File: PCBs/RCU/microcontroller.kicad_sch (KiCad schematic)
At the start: 24 parts, among them J200 USB_C_Receptacle_USB2.0, J201 Conn_01x05, SW201 SW_Push, U200 STM32G0B1CBT6, U201 USBLC6-2SC6, Y200 16MHz

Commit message: Schematic cleanup
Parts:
- C202: value 0.1u -> (none)
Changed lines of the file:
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@@
       (effects (font (size 1.27 1.27)) (justify left))
     )
-    (property "Value" "0.1u" (id 1) (at 180.34 132.0799 0)
+    (property "Value" "" (id 1) (at 180.34 132.0799 0)
       (effects (font (size 1.27 1.27)) (justify left))
     )

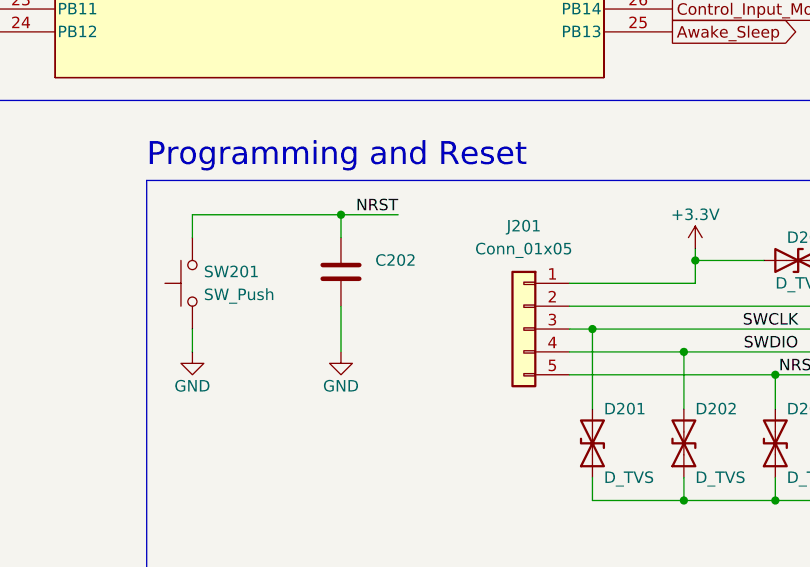
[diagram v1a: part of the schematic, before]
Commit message: Corrected SPI_MOSI and SPI_MISO labels on U700 - external memory
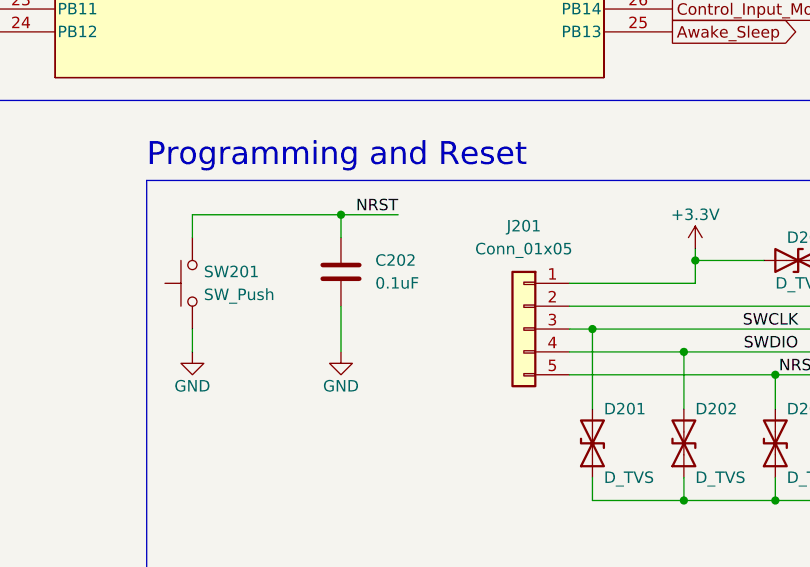
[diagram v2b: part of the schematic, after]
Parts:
- C202: value (none) -> 0.1uF
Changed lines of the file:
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@@
       (effects (font (size 1.27 1.27)) (justify left))
     )
-    (property "Value" "" (id 1) (at 180.34 132.0799 0)
+    (property "Value" "0.1uF" (id 1) (at 180.34 132.0799 0)
       (effects (font (size 1.27 1.27)) (justify left))
     )

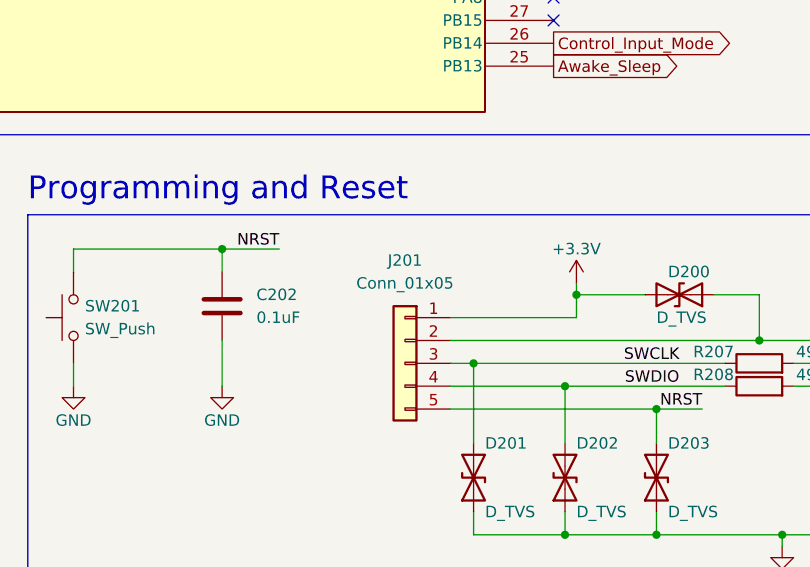
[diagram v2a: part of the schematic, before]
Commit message: Add microcontroller, USB receptable and Connx05 footprints
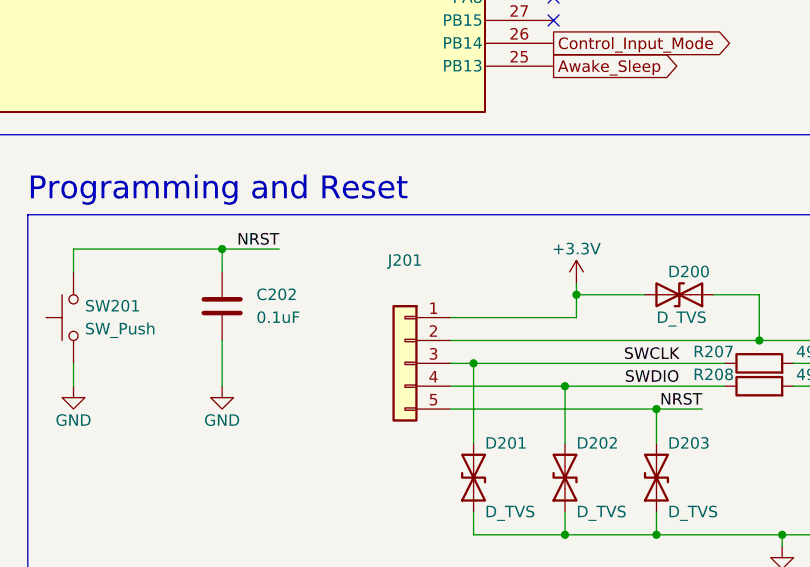
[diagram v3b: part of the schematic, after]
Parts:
- J200: footprint (none) -> Connector_USB:USB_C_Receptacle_HRO_TYPE-C-31-M-12
- J201: value Conn_01x05 -> (none)
- U200: footprint LQFP48_STM32G0B1CBT_STM -> Package_QFP:LQFP-48-1EP_7x7mm_P0.5mm_EP3.6x3.6mm
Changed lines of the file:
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@@
     (in_bom yes) (on_board yes) (fields_autoplaced)
     (property "Reference" "J201" (id 0) (at 196.85 125.73 0))
-    (property "Value" "Conn_01x05" (id 1) (at 196.85 128.27 0))
+    (property "Value" "" (id 1) (at 196.85 128.27 0))
     (property "Footprint" "" (id 2) (at 196.85 137.16 0)
       (effects (font (size 1.27 1.27)) hide)
@@
       (effects (font (size 1.524 1.524)))
     )
-    (property "Footprint" "LQFP48_STM32G0B1CBT_STM" (id 2) (at 137.16 45.72 0)
+    (property "Footprint" "Package_QFP:LQFP-48-1EP_7x7mm_P0.5mm_EP3.6x3.6mm" (id 2) (at 137.16 45.72 0)
       (effects (font (size 1.27 1.27) italic) hide)
     )
@@
     (property "Reference" "J200" (id 0) (at 60.96 133.35 0))
     (property "Value" "USB_C_Receptacle_USB2.0" (id 1) (at 60.96 135.89 0))
-    (property "Footprint" "" (id 2) (at 64.77 156.21 0)
-      (effects (font (size 1.27 1.27)) hide)
-    )
+    (property "Footprint" "Connector_USB:USB_C_Receptacle_HRO_TYPE-C-31-M-12" (id 2) (at 64.77 156.21 0)
+      (effects (font (size 1.27 1.27)) hide)
+    )

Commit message: Add OPA320, DRV8876, Motor Terminal and encoder footprints
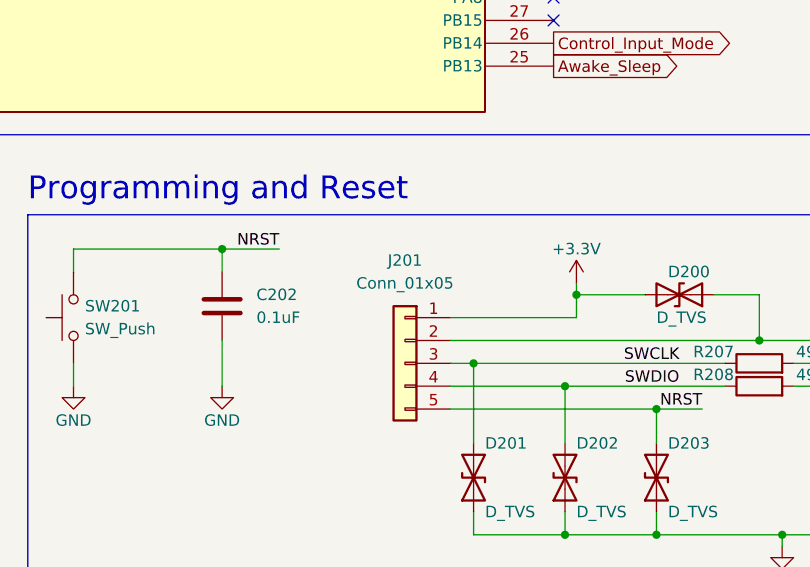
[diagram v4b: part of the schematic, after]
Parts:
- J201: value (none) -> Conn_01x05; footprint (none) -> Connector_PinHeader_2.54mm:PinHeader_1x05_P2.54mm_Vertical
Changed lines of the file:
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@@
     (in_bom yes) (on_board yes) (fields_autoplaced)
     (property "Reference" "J201" (id 0) (at 196.85 125.73 0))
-    (property "Value" "" (id 1) (at 196.85 128.27 0))
-    (property "Footprint" "" (id 2) (at 196.85 137.16 0)
+    (property "Value" "Conn_01x05" (id 1) (at 196.85 128.27 0))
+    (property "Footprint" "Connector_PinHeader_2.54mm:PinHeader_1x05_P2.54mm_Vertical" (id 2) (at 196.85 137.16 0)
       (effects (font (size 1.27 1.27)) hide)
     )

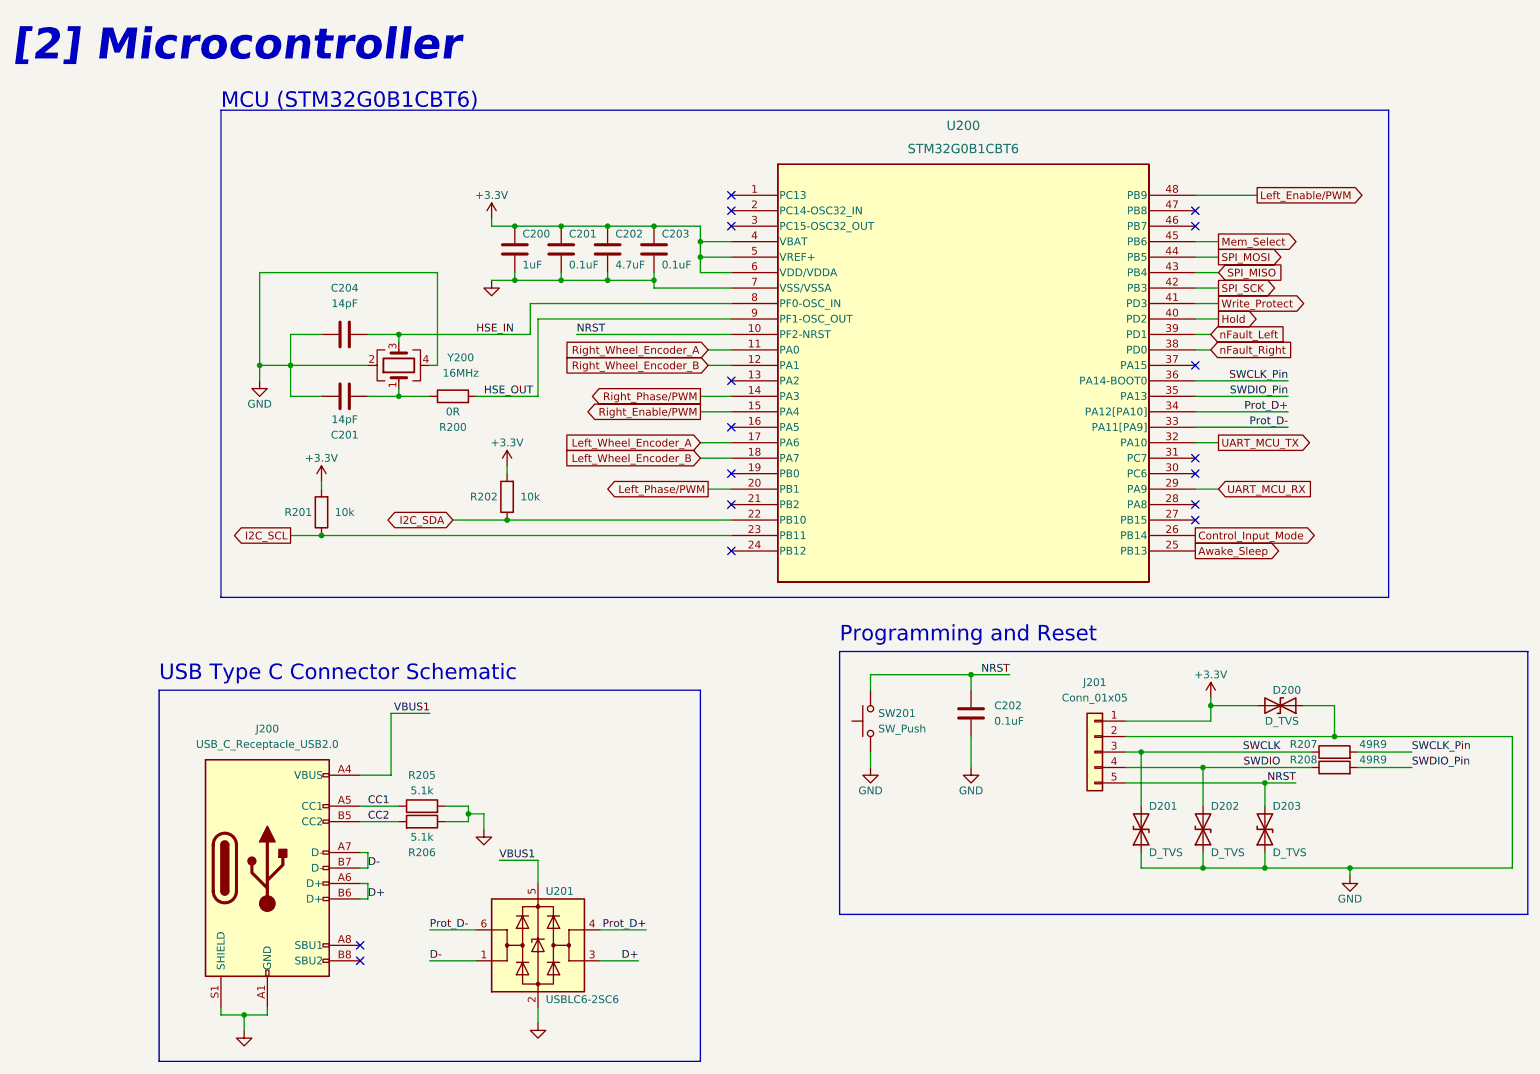
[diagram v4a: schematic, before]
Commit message: Add fooprint for TVS diode, tactile switch and crystal in [2]
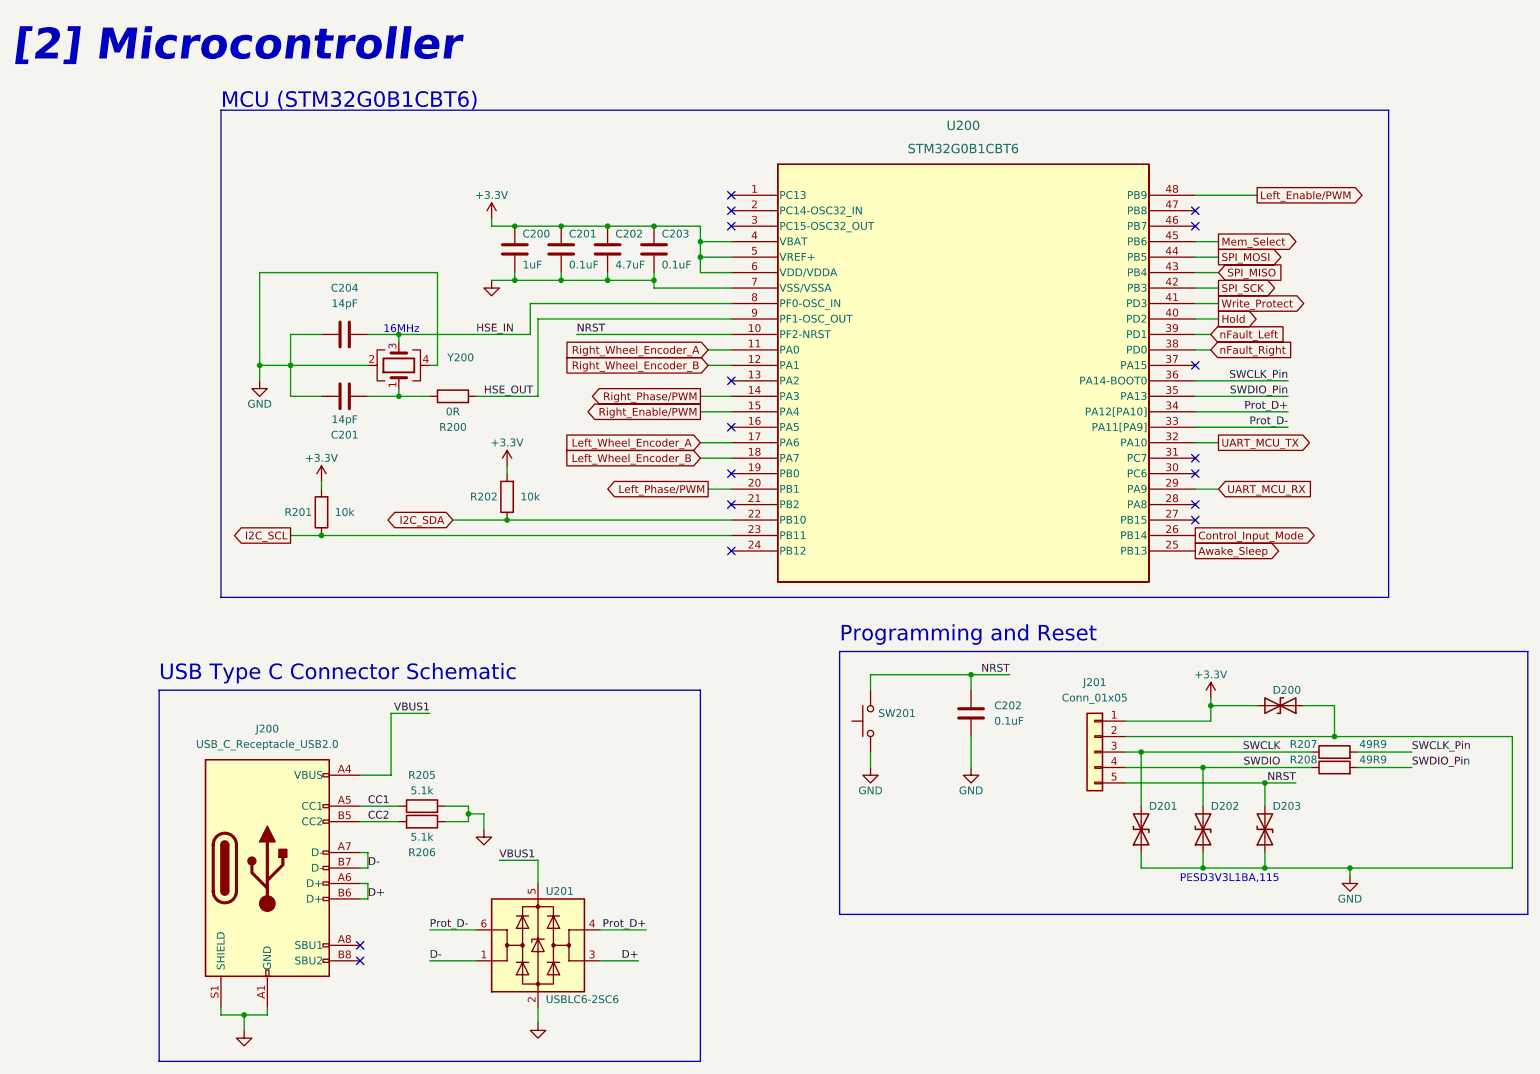
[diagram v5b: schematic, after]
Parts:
- D200, D201, D202, D203: value D_TVS -> (none)
- SW201: value SW_Push -> (none)
- Y200: value 16MHz -> (none)
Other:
- note added: "16MHz"
- note added: "PESD3V3L1BA,115"
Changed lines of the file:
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@@
     (effects (font (size 2.54 2.54)) (justify left bottom))
+  )
+  (text "PESD3V3L1BA,115" (at 210.82 158.75 0)
+    (effects (font (size 1.27 1.27)) (justify left bottom))
+  )
+  (text "16MHz" (at 80.01 68.58 0)
+    (effects (font (size 1.27 1.27)) (justify left bottom))
   )
   (text "USB Type C Connector Schematic" (at 43.18 125.73 0)
@@
       (effects (font (size 1.27 1.27)) (justify right))
     )
-    (property "Value" "SW_Push" (id 1) (at 161.29 133.3499 90)
+    (property "Value" "" (id 1) (at 161.29 133.3499 90)
       (effects (font (size 1.27 1.27)) (justify right))
     )
@@
     (in_bom yes) (on_board yes)
     (property "Reference" "Y200" (id 0) (at 92.71 72.39 90))
-    (property "Value" "16MHz" (id 1) (at 92.71 74.93 90))
+    (property "Value" "" (id 1) (at 92.71 74.93 90))
     (property "Footprint" "" (id 2) (at 82.55 73.66 0)
       (effects (font (size 1.27 1.27)) hide)
@@
       (effects (font (size 1.27 1.27)) (justify right))
     )
-    (property "Value" "D_TVS" (id 1) (at 226.06 153.67 90)
-      (effects (font (size 1.27 1.27)) (justify right))
+    (property "Value" "" (id 1) (at 226.06 153.67 90)
+      (effects (font (size 1.27 1.27)) (justify right) hide)
     )
     (property "Footprint" "" (id 2) (at 224.79 149.86 0)
@@
       (effects (font (size 1.27 1.27)) (justify right))
     )
-    (property "Value" "D_TVS" (id 1) (at 205.74 153.67 90)
-      (effects (font (size 1.27 1.27)) (justify right))
+    (property "Value" "" (id 1) (at 205.74 153.67 90)
+      (effects (font (size 1.27 1.27)) (justify right) hide)
     )
     (property "Footprint" "" (id 2) (at 204.47 149.86 0)
@@
       (effects (font (size 1.27 1.27)) (justify right))
     )
-    (property "Value" "D_TVS" (id 1) (at 215.9 153.67 90)
-      (effects (font (size 1.27 1.27)) (justify right))
+    (property "Value" "" (id 1) (at 215.9 153.67 90)
+      (effects (font (size 1.27 1.27)) (justify right) hide)
     )
     (property "Footprint" "" (id 2) (at 214.63 149.86 0)
@@
       (effects (font (size 1.27 1.27)) (justify right))
     )
-    (property "Value" "D_TVS" (id 1) (at 224.79 132.08 0)
-      (effects (font (size 1.27 1.27)) (justify right))
+    (property "Value" "" (id 1) (at 224.79 132.08 0)
+      (effects (font (size 1.27 1.27)) (justify right) hide)
     )
     (property "Footprint" "" (id 2) (at 227.33 129.54 0)
